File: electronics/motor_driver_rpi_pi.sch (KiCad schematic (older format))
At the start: 9 parts

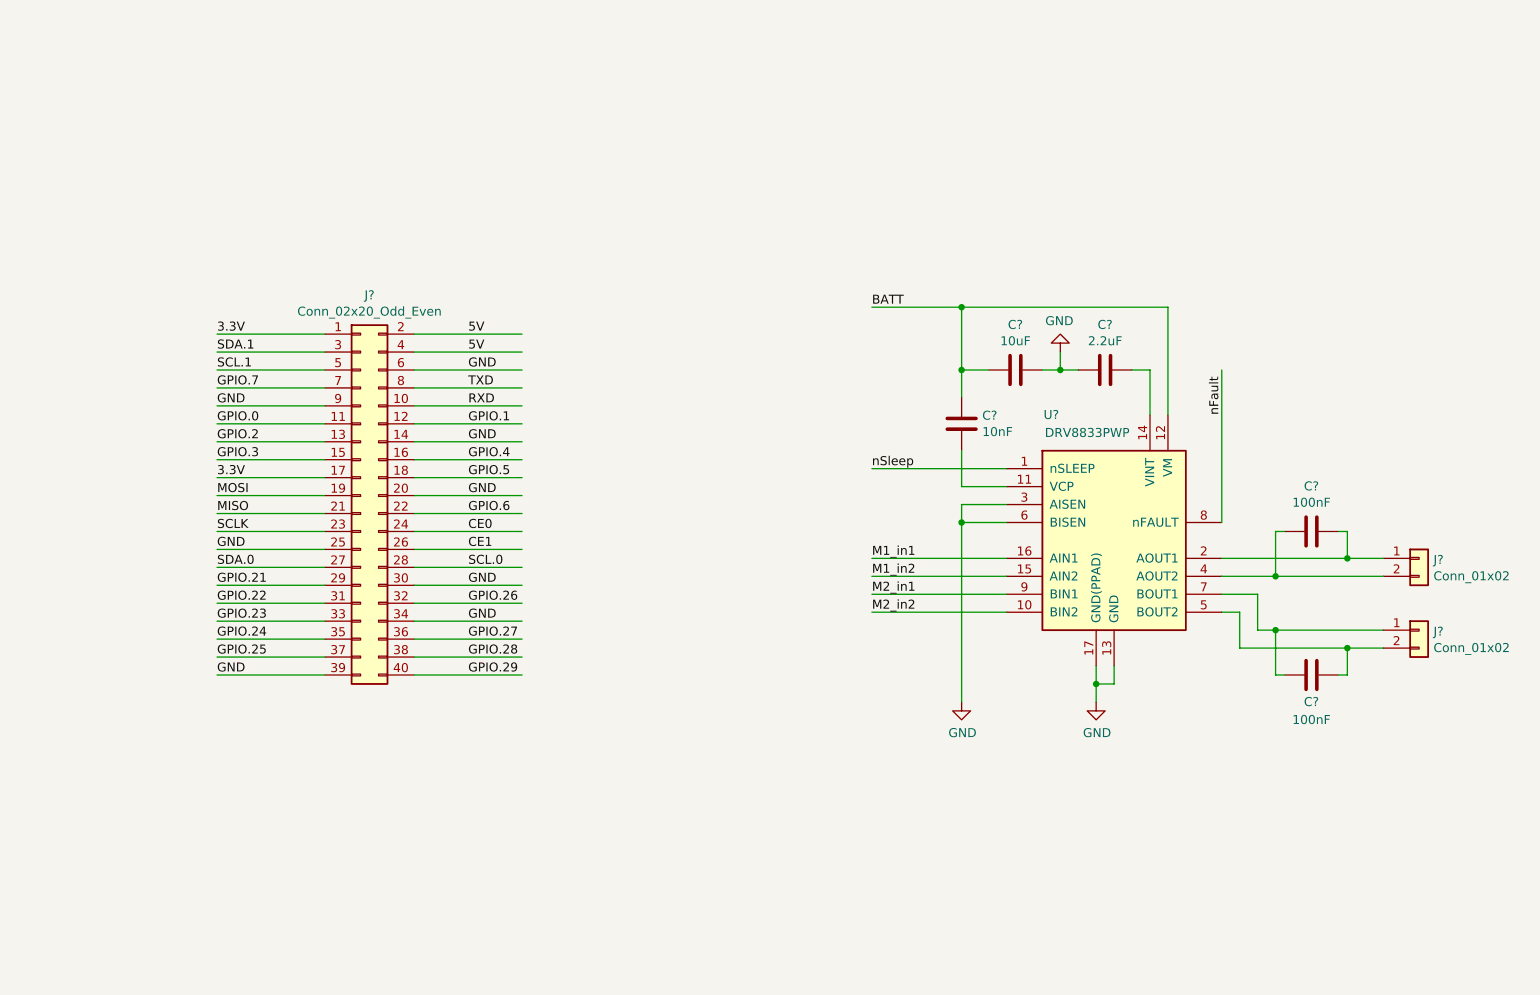
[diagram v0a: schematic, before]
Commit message: Preview SCH is done, but not fully finished.
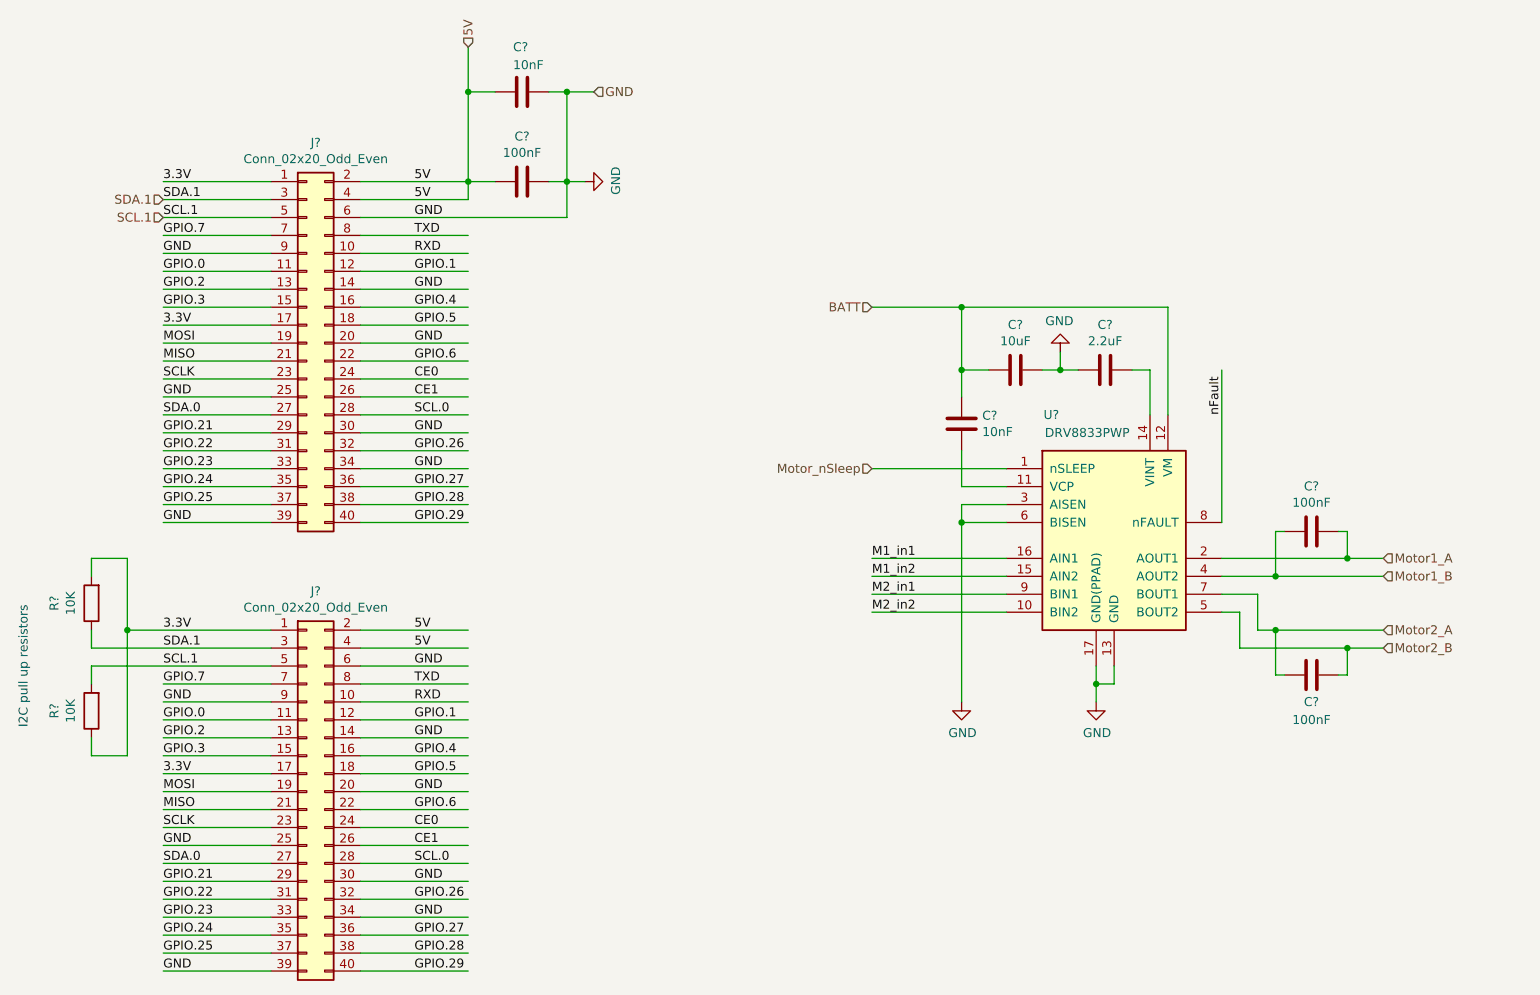
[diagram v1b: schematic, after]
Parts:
- removed J? (x2): Conn_01x02, Connector_Wire:SolderWirePad_1x02_P3.81mm_Drill0.8mm, symbol Connector_Generic:Conn_01x02
- added C?: 10nF, symbol Device:C
- added C?: 100nF, symbol Device:C
- added J?: Conn_02x20_Odd_Even, symbol Connector_Generic:Conn_02x20_Odd_Even
- added R? (x2): 10K, Resistor_SMD:R_0805_2012Metric, symbol Device:R
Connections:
- net labels added: Motor1_A, Motor1_B, Motor2_A, Motor2_B, Motor_nSleep
- net labels removed: nSleep
- wire segments 87 -> 146
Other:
- note added: "I2C pull up resistors"
- moved on the sheet: J?

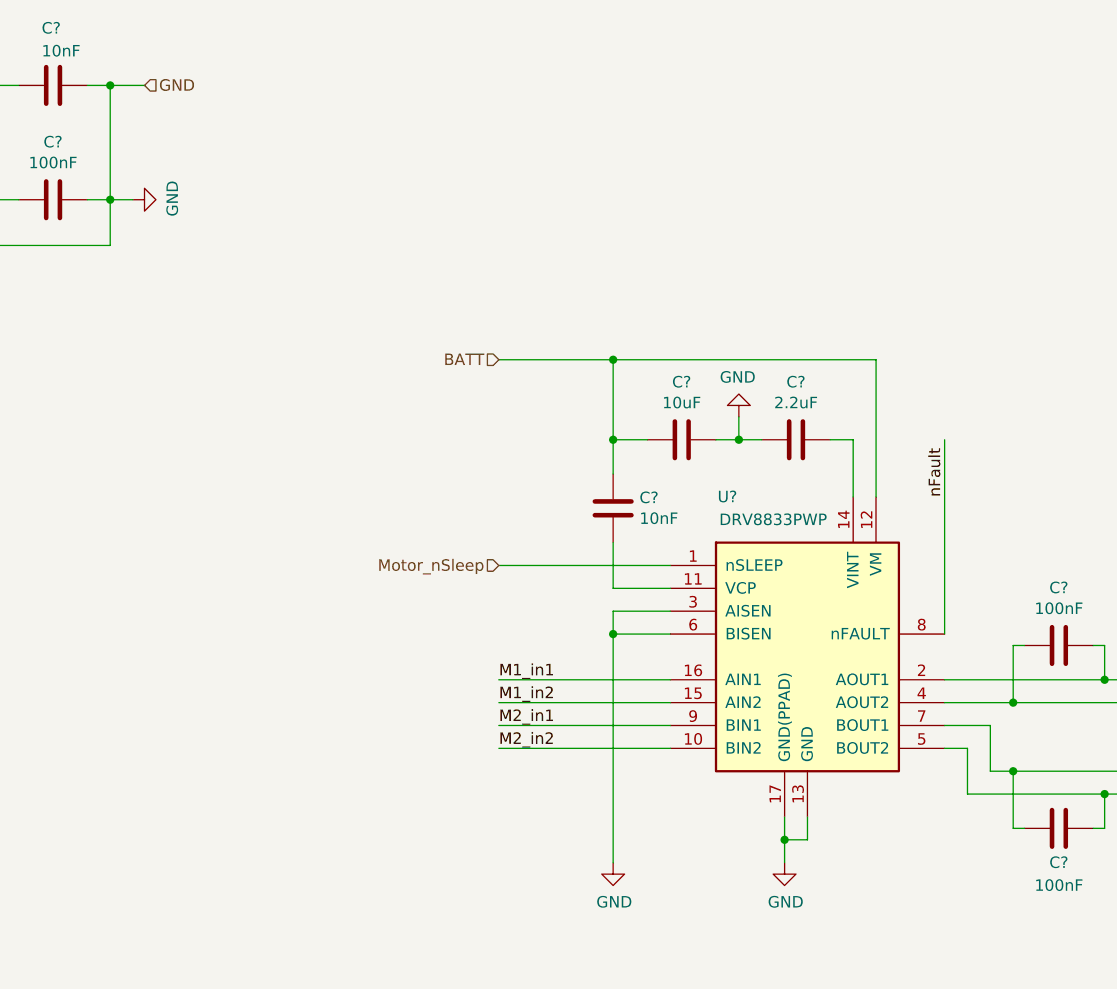
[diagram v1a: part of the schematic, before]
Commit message: Electronics define IOs to motor driver.
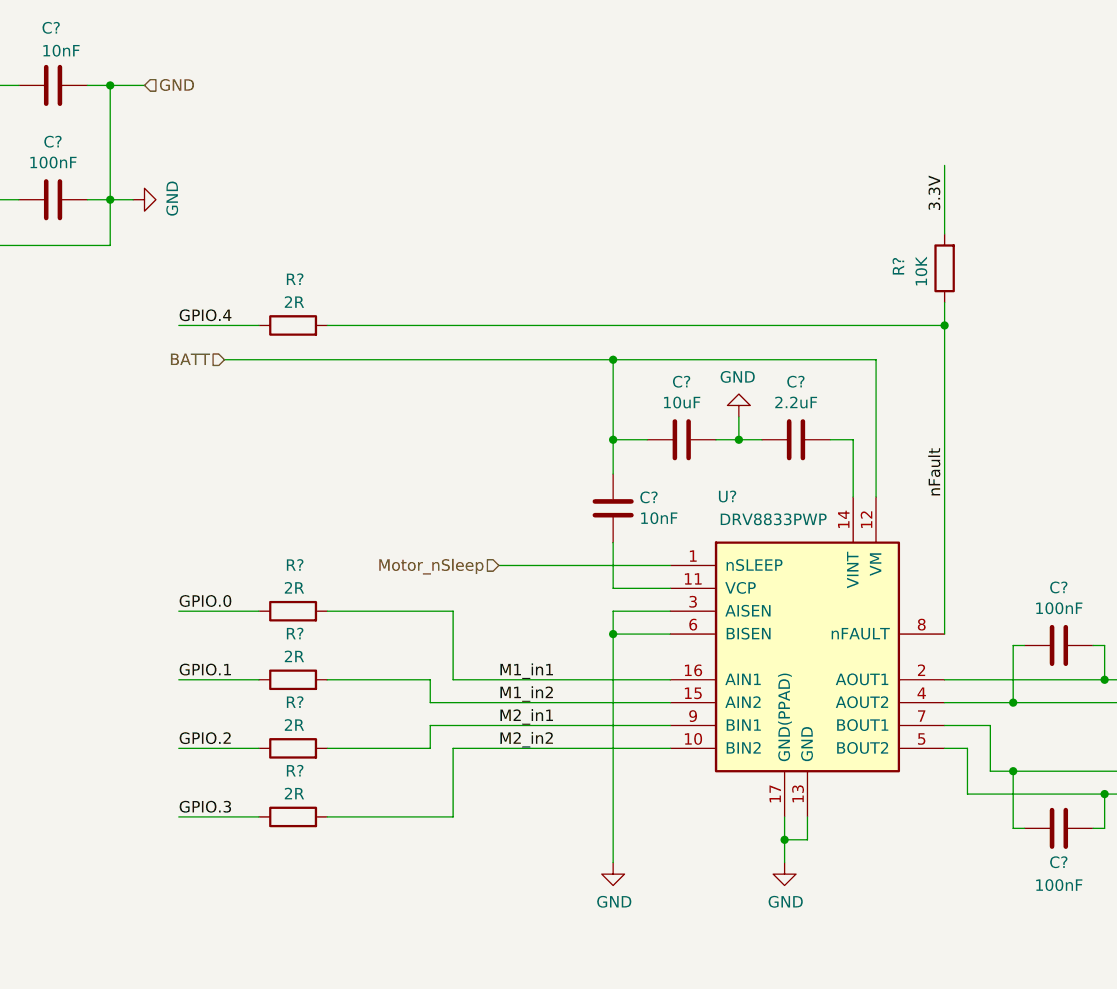
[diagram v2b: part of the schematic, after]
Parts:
- added R? (x5): 2R, Resistor_SMD:R_0805_2012Metric, symbol Device:R
- added R?: 10K, Resistor_SMD:R_0805_2012Metric, symbol Device:R
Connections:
- wire segments 146 -> 162
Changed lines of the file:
@@
 $Descr A4 11693 8268
 encoding utf-8
-Sheet 3 4
+Sheet 2 4
 Title ""
 Date ""
@@
 $EndComp
 Wire Wire Line
-	7150 4250 6400 4250
-Wire Wire Line
-	7150 4350 6400 4350
-Wire Wire Line
-	7150 4450 6400 4450
-Wire Wire Line
-	7150 4550 6400 4550
-Wire Wire Line
 	7650 4850 7650 4950
 Wire Wire Line
@@
 Wire Wire Line
 	7450 3200 7550 3200
-Wire Wire Line
-	7150 3750 6400 3750
 Text Label 8350 3450 1    50   ~ 0
 nFault
@@
 	3050 3950 2450 3950
 Wire Wire Line
-	6400 2850 6900 2850
+	5200 2850 6900 2850
 Wire Wire Line
 	6900 3350 6900 3200
@@
 Wire Wire Line
 	6900 4050 6900 3950
-Wire Wire Line
-	8350 4050 8350 3200
 Wire Wire Line
 	8350 4250 9050 4250
@@
 Text HLabel 9250 4750 2    50   Input ~ 0
 Motor2_B
-Text HLabel 6400 2850 0    50   Input ~ 0
+Text HLabel 5200 2850 0    50   Input ~ 0
 BATT
 Wire Wire Line
@@
 Text HLabel 4150 1400 1    50   Input ~ 0
 5V
-Text HLabel 6400 3750 0    50   Input ~ 0
-Motor_nSleep
 Text HLabel 2450 2250 0    50   Input ~ 0
 SDA.1
@@
 Text Notes 1700 5200 1    50   ~ 0
 I2C pull up resistors
+$Comp
+L Device:R R?
+U 1 1 5E968EC1
+P 5500 3950
+F 0 "R?" V 5700 3900 50  0000 L CNN
+F 1 "2R" V 5600 3900 50  0000 L CNN
+F 2 "Resistor_SMD:R_0805_2012Metric" V 5430 3950 50  0001 C CNN
+F 3 "~" H 5500 3950 50  0001 C CNN
+	1    5500 3950
+	0    -1   -1   0
+$EndComp
+$Comp
+L Device:R R?
+U 1 1 5E97A58B
+P 5500 4250
+F 0 "R?" V 5700 4200 50  0000 L CNN
+F 1 "2R" V 5600 4200 50  0000 L CNN
+F 2 "Resistor_SMD:R_0805_2012Metric" V 5430 4250 50  0001 C CNN
+F 3 "~" H 5500 4250 50  0001 C CNN
+	1    5500 4250
+	0    -1   -1   0
+$EndComp
+$Comp
+L Device:R R?
+U 1 1 5E98311B
+P 5500 4550
+F 0 "R?" V 5700 4500 50  0000 L CNN
+F 1 "2R" V 5600 4500 50  0000 L CNN
+F 2 "Resistor_SMD:R_0805_2012Metric" V 5430 4550 50  0001 C CNN
+F 3 "~" H 5500 4550 50  0001 C CNN
+	1    5500 4550
+	0    -1   -1   0
+$EndComp
+$Comp
+L Device:R R?
+U 1 1 5E98BD49
+P 5500 4850
+AR Path="/5E915994/5E98BD49" Ref="R?"  Part="1"
+AR Path="/5E914BA5/5E98BD49" Ref="R?"  Part="1"
+F 0 "R?" V 5700 4800 50  0000 L CNN
+F 1 "2R" V 5600 4800 50  0000 L CNN
+F 2 "Resistor_SMD:R_0805_2012Metric" V 5430 4850 50  0001 C CNN
+F 3 "~" H 5500 4850 50  0001 C CNN
+	1    5500 4850
+	0    -1   -1   0
+$EndComp
+Wire Wire Line
+	5350 3950 5000 3950
+Wire Wire Line
+	5350 4250 5000 4250
+Wire Wire Line
+	5350 4550 5000 4550
+Wire Wire Line
+	5350 4850 5000 4850
+Wire Wire Line
+	5650 4250 6100 4250
+Wire Wire Line
+	6100 4250 6100 4350
+Wire Wire Line
+	6100 4350 7150 4350
+Wire Wire Line
+	5650 4550 6100 4550
+Wire Wire Line
+	6100 4550 6100 4450
+Wire Wire Line
+	6100 4450 7150 4450
+Wire Wire Line
+	5650 3950 6200 3950
+Wire Wire Line
+	6200 3950 6200 4250
+Wire Wire Line
+	6200 4250 7150 4250
+Wire Wire Line
+	5650 4850 6200 4850
+Wire Wire Line
+	6200 4850 6200 4550
+Wire Wire Line
+	6200 4550 7150 4550
+$Comp
+L Device:R R?
+U 1 1 5EA10DA4
+P 5500 2700
+AR Path="/5E915994/5EA10DA4" Ref="R?"  Part="1"
+AR Path="/5E914BA5/5EA10DA4" Ref="R?"  Part="1"
+F 0 "R?" V 5700 2650 50  0000 L CNN
+F 1 "2R" V 5600 2650 50  0000 L CNN
+F 2 "Resistor_SMD:R_0805_2012Metric" V 5430 2700 50  0001 C CNN
+F 3 "~" H 5500 2700 50  0001 C CNN
+	1    5500 2700
+	0    -1   -1   0
+$EndComp
+Wire Wire Line
+	8350 2700 5650 2700
+Wire Wire Line
+	8350 2700 8350 4050
+Wire Wire Line
+	5350 2700 5000 2700
+$Comp
+L Device:R R?
+U 1 1 5EA4BBA6
+P 8350 2450
+AR Path="/5E915994/5EA4BBA6" Ref="R?"  Part="1"
+AR Path="/5E914BA5/5EA4BBA6" Ref="R?"  Part="1"
+F 0 "R?" V 8550 2400 50  0000 L CNN
+F 1 "10K" V 8450 2400 50  0000 L CNN
+F 2 "Resistor_SMD:R_0805_2012Metric" V 8280 2450 50  0001 C CNN
+F 3 "~" H 8350 2450 50  0001 C CNN
+	1    8350 2450
+	-1   0    0    1
+$EndComp
+Wire Wire Line
+	8350 2700 8350 2600
+Connection ~ 8350 2700
+Wire Wire Line
+	8350 2000 8350 2300
+Text Label 8350 2200 1    50   ~ 0
+3.3V
+Text Label 5000 3950 0    50   ~ 0
+GPIO.0
+Text Label 5000 4250 0    50   ~ 0
+GPIO.1
+Text Label 5000 4550 0    50   ~ 0
+GPIO.2
+Text Label 5000 4850 0    50   ~ 0
+GPIO.3
+Text Label 5000 2700 0    50   ~ 0
+GPIO.4
+Wire Wire Line
+	7150 3750 6400 3750
+Text HLabel 6400 3750 0    50   Input ~ 0
+Motor_nSleep
 $EndSCHEMATC

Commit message: modified:   ../../electronics/charger.sch 	modified:   ../../electronics/charger.sch-bak 	modified:   ../../electronics/dc_dc.sch 	modified:   ../../electronics/dc_dc.sch-bak 	modified:   ../../electronics/langpie.pro 	modified:   ../../electronics/langpie.sch 	modified:   ../../electronics/langpie.sch-bak 	modified:   ../../electronics/motor_driver_rpi_pi.sch 	modified:   ../../electronics/motor_driver_rpi_pi.sch-bak 	modified:   ../../electronics/schematic_v1_preview.pdf
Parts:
- R10, R11, R7, R8, R9: renamed from R?; value 2R -> 200R
- gave numbers to parts that had none: 13
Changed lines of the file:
@@
 $EndDescr
 $Comp
-L Driver_Motor:DRV8833PWP U?
+L Driver_Motor:DRV8833PWP U1
 U 1 1 5E914FDC
 P 7750 4150
-F 0 "U?" H 7400 4850 50  0000 C CNN
+F 0 "U1" H 7400 4850 50  0000 C CNN
 F 1 "DRV8833PWP" H 7600 4750 50  0000 C CNN
 F 2 "Package_SO:HTSSOP-16-1EP_4.4x5mm_P0.65mm_EP3.4x5mm_Mask2.46x2.31mm_ThermalVias" H 8200 4600 50  0001 L CNN
@@
 	8550 4450 8550 4650
 $Comp
-L Device:C C?
+L Device:C C5
 U 1 1 5E91DB31
 P 7700 3200
-F 0 "C?" V 7448 3200 50  0000 C CNN
+F 0 "C5" V 7448 3200 50  0000 C CNN
 F 1 "2.2uF" V 7539 3200 50  0000 C CNN
 F 2 "" H 7738 3050 50  0001 C CNN
@@
 	8050 3450 8050 2850
 $Comp
-L Device:C C?
+L Device:C C4
 U 1 1 5E921668
 P 7200 3200
-F 0 "C?" V 6948 3200 50  0000 C CNN
+F 0 "C4" V 6948 3200 50  0000 C CNN
 F 1 "10uF" V 7039 3200 50  0000 C CNN
 F 2 "" H 7238 3050 50  0001 C CNN
@@
 M2_in2
 $Comp
-L Device:C C?
+L Device:C C7
 U 1 1 5E99371A
 P 8850 4900
-F 0 "C?" V 9000 4900 50  0000 C CNN
+F 0 "C7" V 9000 4900 50  0000 C CNN
 F 1 "100nF" V 9100 4900 50  0000 C CNN
 F 2 "" H 8888 4750 50  0001 C CNN
@@
 $EndComp
 $Comp
-L Device:C C?
+L Device:C C6
 U 1 1 5E994290
 P 8850 4100
-F 0 "C?" V 8598 4100 50  0000 C CNN
+F 0 "C6" V 8598 4100 50  0000 C CNN
 F 1 "100nF" V 8689 4100 50  0000 C CNN
 F 2 "" H 8888 3950 50  0001 C CNN
@@
 	9050 4750 9250 4750
 $Comp
-L Device:C C?
+L Device:C C3
 U 1 1 5E920233
 P 6900 3500
-F 0 "C?" H 7015 3546 50  0000 L CNN
+F 0 "C3" H 7015 3546 50  0000 L CNN
 F 1 "10nF" H 7015 3455 50  0000 L CNN
 F 2 "" H 6938 3350 50  0001 C CNN
@@
 P 3250 3050
 AR Path="/5E9108BA/5E9AD554" Ref="J?"  Part="1"
-AR Path="/5E914BA5/5E9AD554" Ref="J?"  Part="1"
-F 0 "J?" H 3300 4167 50  0000 C CNN
+AR Path="/5E914BA5/5E9AD554" Ref="J5"  Part="1"
+F 0 "J5" H 3300 4167 50  0000 C CNN
 F 1 "Conn_02x20_Odd_Even" H 3300 4076 50  0000 C CNN
 F 2 "" H 3250 3050 50  0001 C CNN
@@
 SCL.1
 $Comp
-L Device:C C?
+L Device:C C1
 U 1 1 5EAFE5F1
 P 4450 1650
-F 0 "C?" V 4200 1600 50  0000 L CNN
+F 0 "C1" V 4200 1600 50  0000 L CNN
 F 1 "10nF" V 4300 1600 50  0000 L CNN
 F 2 "" H 4488 1500 50  0001 C CNN
@@
 $EndComp
 $Comp
-L Device:C C?
+L Device:C C2
 U 1 1 5EB01D5C
 P 4450 2150
-F 0 "C?" V 4198 2150 50  0000 C CNN
+F 0 "C2" V 4198 2150 50  0000 C CNN
 F 1 "100nF" V 4289 2150 50  0000 C CNN
 F 2 "" H 4488 2000 50  0001 C CNN
@@
 P 3250 5550
 AR Path="/5E9108BA/5EB478CD" Ref="J?"  Part="1"
-AR Path="/5E914BA5/5EB478CD" Ref="J?"  Part="1"
-F 0 "J?" H 3300 6667 50  0000 C CNN
+AR Path="/5E914BA5/5EB478CD" Ref="J6"  Part="1"
+F 0 "J6" H 3300 6667 50  0000 C CNN
 F 1 "Conn_02x20_Odd_Even" H 3300 6576 50  0000 C CNN
 F 2 "" H 3250 5550 50  0001 C CNN
@@
 AR Path="/5E90B2B2/5EC16629" Ref="R?"  Part="1"
 AR Path="/5EC16629" Ref="R?"  Part="1"
-AR Path="/5E914BA5/5EC16629" Ref="R?"  Part="1"
-F 0 "R?" V 2257 4500 50  0000 C CNN
+AR Path="/5E914BA5/5EC16629" Ref="R5"  Part="1"
+F 0 "R5" V 2257 4500 50  0000 C CNN
 F 1 "10K" V 2166 4500 50  0000 C CNN
 F 2 "Resistor_SMD:R_0805_2012Metric" V 1980 4500 50  0001 C CNN
@@
 AR Path="/5E90B2B2/5EC1EC79" Ref="R?"  Part="1"
 AR Path="/5EC1EC79" Ref="R?"  Part="1"
-AR Path="/5E914BA5/5EC1EC79" Ref="R?"  Part="1"
-F 0 "R?" V 2257 5100 50  0000 C CNN
+AR Path="/5E914BA5/5EC1EC79" Ref="R6"  Part="1"
+F 0 "R6" V 2257 5100 50  0000 C CNN
 F 1 "10K" V 2166 5100 50  0000 C CNN
 F 2 "Resistor_SMD:R_0805_2012Metric" V 1980 5100 50  0001 C CNN
@@
 I2C pull up resistors
 $Comp
-L Device:R R?
+L Device:R R8
 U 1 1 5E968EC1
 P 5500 3950
-F 0 "R?" V 5700 3900 50  0000 L CNN
-F 1 "2R" V 5600 3900 50  0000 L CNN
+F 0 "R8" V 5700 3900 50  0000 L CNN
+F 1 "200R" V 5600 3900 50  0000 L CNN
 F 2 "Resistor_SMD:R_0805_2012Metric" V 5430 3950 50  0001 C CNN
 F 3 "~" H 5500 3950 50  0001 C CNN
@@
 $EndComp
 $Comp
-L Device:R R?
+L Device:R R9
 U 1 1 5E97A58B
 P 5500 4250
-F 0 "R?" V 5700 4200 50  0000 L CNN
-F 1 "2R" V 5600 4200 50  0000 L CNN
+F 0 "R9" V 5700 4200 50  0000 L CNN
+F 1 "200R" V 5600 4200 50  0000 L CNN
 F 2 "Resistor_SMD:R_0805_2012Metric" V 5430 4250 50  0001 C CNN
 F 3 "~" H 5500 4250 50  0001 C CNN
@@
 $EndComp
 $Comp
-L Device:R R?
+L Device:R R10
 U 1 1 5E98311B
 P 5500 4550
-F 0 "R?" V 5700 4500 50  0000 L CNN
-F 1 "2R" V 5600 4500 50  0000 L CNN
+F 0 "R10" V 5700 4500 50  0000 L CNN
+F 1 "200R" V 5600 4500 50  0000 L CNN
 F 2 "Resistor_SMD:R_0805_2012Metric" V 5430 4550 50  0001 C CNN
 F 3 "~" H 5500 4550 50  0001 C CNN
@@
 P 5500 4850
 AR Path="/5E915994/5E98BD49" Ref="R?"  Part="1"
-AR Path="/5E914BA5/5E98BD49" Ref="R?"  Part="1"
-F 0 "R?" V 5700 4800 50  0000 L CNN
-F 1 "2R" V 5600 4800 50  0000 L CNN
+AR Path="/5E914BA5/5E98BD49" Ref="R11"  Part="1"
+F 0 "R11" V 5700 4800 50  0000 L CNN
+F 1 "200R" V 5600 4800 50  0000 L CNN
 F 2 "Resistor_SMD:R_0805_2012Metric" V 5430 4850 50  0001 C CNN
 F 3 "~" H 5500 4850 50  0001 C CNN
@@
 P 5500 2700
 AR Path="/5E915994/5EA10DA4" Ref="R?"  Part="1"
-AR Path="/5E914BA5/5EA10DA4" Ref="R?"  Part="1"
-F 0 "R?" V 5700 2650 50  0000 L CNN
-F 1 "2R" V 5600 2650 50  0000 L CNN
+AR Path="/5E914BA5/5EA10DA4" Ref="R7"  Part="1"
+F 0 "R7" V 5700 2650 50  0000 L CNN
+F 1 "200R" V 5600 2650 50  0000 L CNN
 F 2 "Resistor_SMD:R_0805_2012Metric" V 5430 2700 50  0001 C CNN
 F 3 "~" H 5500 2700 50  0001 C CNN
@@
 P 8350 2450
 AR Path="/5E915994/5EA4BBA6" Ref="R?"  Part="1"
-AR Path="/5E914BA5/5EA4BBA6" Ref="R?"  Part="1"
-F 0 "R?" V 8550 2400 50  0000 L CNN
+AR Path="/5E914BA5/5EA4BBA6" Ref="R12"  Part="1"
+F 0 "R12" V 8550 2400 50  0000 L CNN
 F 1 "10K" V 8450 2400 50  0000 L CNN
 F 2 "Resistor_SMD:R_0805_2012Metric" V 8280 2450 50  0001 C CNN
